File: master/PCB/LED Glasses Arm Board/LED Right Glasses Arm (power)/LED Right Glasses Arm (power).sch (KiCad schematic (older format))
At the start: 26 parts, among them J1 Conn_01x02_Male, J2 Conn_01x01_Male, J3 Conn_01x01_Male, Q1 TP0610T, SW1 SW_SPST, U1 TPS63061DSCT

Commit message: Changes
Test points, routing, need to get the ground plane on the back copper
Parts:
- TP_gnd1, TP_input_voltage1, TP_output_voltage1: footprint Connector_PinHeader_1.00mm:PinHeader_1x01_P1.00mm_Vertical_SMD_CUSTOM -> TestPoint:TestPoint_Pad_D1.5mm
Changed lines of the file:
@@
 F 0 "TP_output_voltage1" H 10058 4170 50  0000 L CNN
 F 1 "TestPoint" H 10058 4079 50  0000 L CNN
-F 2 "Connector_PinHeader_1.00mm:PinHeader_1x01_P1.00mm_Vertical_SMD_CUSTOM" H 10200 4050 50  0001 C CNN
+F 2 "TestPoint:TestPoint_Pad_D1.5mm" H 10200 4050 50  0001 C CNN
 F 3 "~" H 10200 4050 50  0001 C CNN
 	1    10000 4050
@@
 F 0 "TP_input_voltage1" H 2408 4120 50  0000 L CNN
 F 1 "TestPoint" H 2408 4029 50  0000 L CNN
-F 2 "Connector_PinHeader_1.00mm:PinHeader_1x01_P1.00mm_Vertical_SMD_CUSTOM" H 2550 4000 50  0001 C CNN
+F 2 "TestPoint:TestPoint_Pad_D1.5mm" H 2550 4000 50  0001 C CNN
 F 3 "~" H 2550 4000 50  0001 C CNN
 	1    2350 4000
@@
 F 0 "TP_gnd1" H 5108 5470 50  0000 L CNN
 F 1 "TestPoint" H 5108 5379 50  0000 L CNN
-F 2 "Connector_PinHeader_1.00mm:PinHeader_1x01_P1.00mm_Vertical_SMD_CUSTOM" H 5250 5350 50  0001 C CNN
+F 2 "TestPoint:TestPoint_Pad_D1.5mm" H 5250 5350 50  0001 C CNN
 F 3 "~" H 5250 5350 50  0001 C CNN
 	1    5050 5350

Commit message: Made a few small cosmetic changes to labels and values (i.e. R_small_US1 to R1).
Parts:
- C1, C4, C7, C8: value 220uF -> 220u; Digikey Link (none) -> https://www.digikey.com.au/product-detail/en/samsung-electr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; Link https://www.digikey.com.au/product-detail/en/samsung-electr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 -> (none)
- C2: Digikey Link (none) -> https://www.digikey.com.au/product-detail/en/samsung-electr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; Link https://www.digikey.com.au/product-detail/en/samsung-electr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 -> (none)
- C3: value 10pF -> 10p; Digikey Link (none) -> https://www.digikey.com.au/product-detail/en/avx-corporatio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; Link https://www.digikey.com.au/product-detail/en/avx-corporatio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 -> (none)
- C5: value 22uF -> 22u; Digikey Link (none) -> https://www.digikey.com.au/product-detail/en/kemet/C0805C22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; Link https://www.digikey.com.au/product-detail/en/kemet/C0805C22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 -> (none)
- C6: value 68uF -> 68u; Digikey Link (none) -> https://www.digikey.com.au/product-detail/en/tdk-corporatio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; Link https://www.digikey.com.au/product-detail/en/tdk-corporatio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 -> (none)
- D1: renamed from D_Zener_Small1; Digikey Link (none) -> https://www.digikey.com.au/product-detail/en/vishay-general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; Digikey link https://www.digikey.com.au/product-detail/en/vishay-general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 -> (none)
- D2: value LED Red -> P_IN
- D3: value LED Green -> P_OUT
- J1: value Conn_01x02_Male -> PWR IN
- J2: value Conn_01x01_Male -> PWR OUT +
- J3: value Conn_01x01_Male -> PWR OUT -
- L1: value 1uF -> 1u; Digikey https://www.digikey.com/en/products/detail/bourns-inc/SRN40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 -> (none); Digikey Link (none) -> https://www.digikey.com/en/products/detail/bourns-inc/SRN40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
- R1: renamed from R_Small_US1; symbol Device:R_Small_US -> LED-Right-Glasses-Arm-(power)-rescue:R_Small_US-Device
- R2, R3, R4, R6: symbol Device:R_Small_US -> LED-Right-Glasses-Arm-(power)-rescue:R_Small_US-Device
- SW1: value SW_SPST -> EN
- TP1: renamed from TP_input_voltage1; value TestPoint -> VIN
- TP2: renamed from TP_gnd1; value TestPoint -> GND
- TP3: renamed from TP_output_voltage1; value TestPoint -> VOUT

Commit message: All changes apply to schematic only and not to the layout. Removed external feedback loop, replaced bulk output capacitance with 3x22uF caps for cost savings and removed led indicator on input power.
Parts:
- removed C1, C4, C7, C8: 220u, Capacitor_SMD:C_1210_3225Metric, symbol Device:C_Small
- removed C3: 10p, Capacitor_SMD:C_0603_1608Metric, symbol Device:C_Small
- removed D2: P_IN, LED_SMD:LED_0603_1608Metric, symbol Device:LED
- removed R2: 2k2, Resistor_SMD:R_0603_1608Metric, symbol LED-Right-Glasses-Arm-(power)-rescue:R_Small_US-Device
- removed R3: 1M, Resistor_SMD:R_0603_1608Metric, symbol LED-Right-Glasses-Arm-(power)-rescue:R_Small_US-Device
- removed R4: 111k, Resistor_SMD:R_0805_2012Metric, symbol LED-Right-Glasses-Arm-(power)-rescue:R_Small_US-Device
- added C? (x2): 22u, Capacitor_SMD:C_1206_3216Metric, symbol Device:C_Small
- added R2: 100k, Resistor_SMD:R_0603_1608Metric, symbol Device:R_Small
- C5: Digikey Link https://www.digikey.com.au/product-detail/en/kemet/C0805C22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 -> https://www.digikey.com.au/product-detail/en/samsung-electr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
- C6: value 68u -> 22u; Digikey Link https://www.digikey.com.au/product-detail/en/tdk-corporatio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 -> https://www.digikey.com.au/product-detail/en/samsung-electr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
- L1: Digikey Link https://www.digikey.com/en/products/detail/bourns-inc/SRN40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 -> https://www.digikey.com.au/product-detail/en/taiyo-yuden/NR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; Old product XFL4020-102MEC -> (none)
- R1: value 100k1 -> 100k; symbol LED-Right-Glasses-Arm-(power)-rescue:R_Small_US-Device -> Device:R_Small
- R6: symbol LED-Right-Glasses-Arm-(power)-rescue:R_Small_US-Device -> Device:R_Small
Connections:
- net labels added: 5V0
- net labels removed: VOUT_5V
- wire segments 64 -> 42
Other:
- moved on the sheet: C2, C5, C6, D3, J2, J3, SW1, TP2, TP3

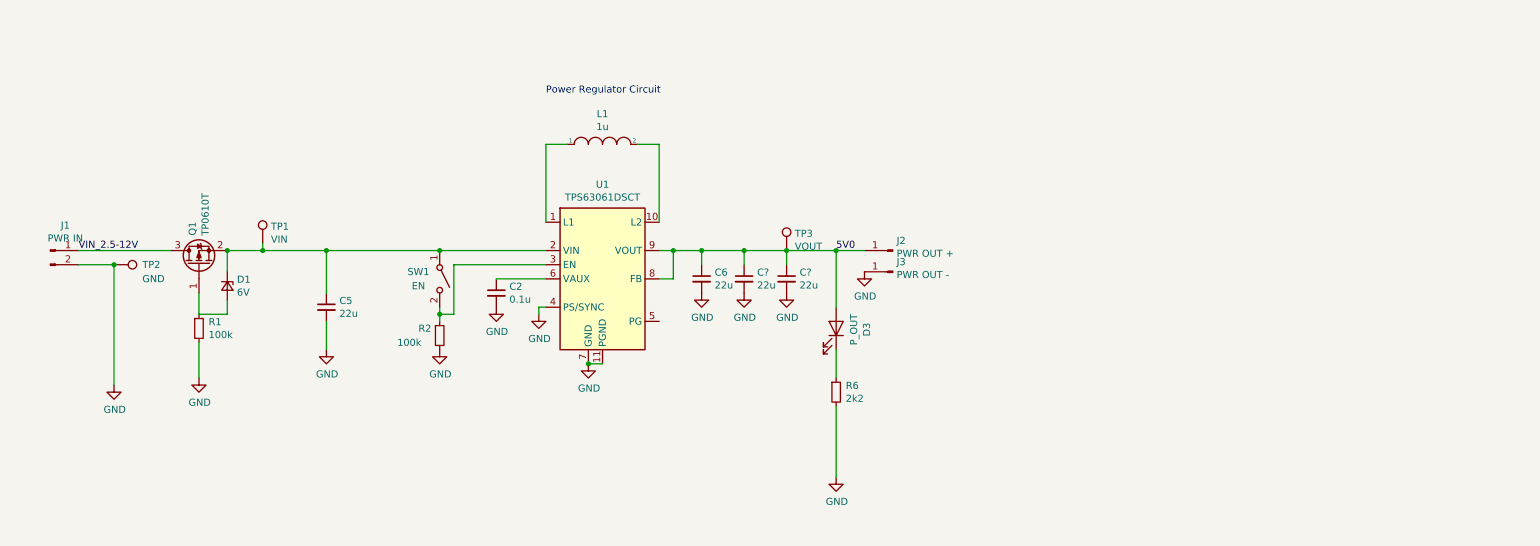
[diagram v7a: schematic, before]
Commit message: Changed LED indicator from 5V out to PG from power reg IC, moved annotation from 0-x to 100-1xx to keep it consistent with mcu arm design, adjusted layout to accomodate schematic changes from this commit and the previous and added silkscreen labels to input and output.
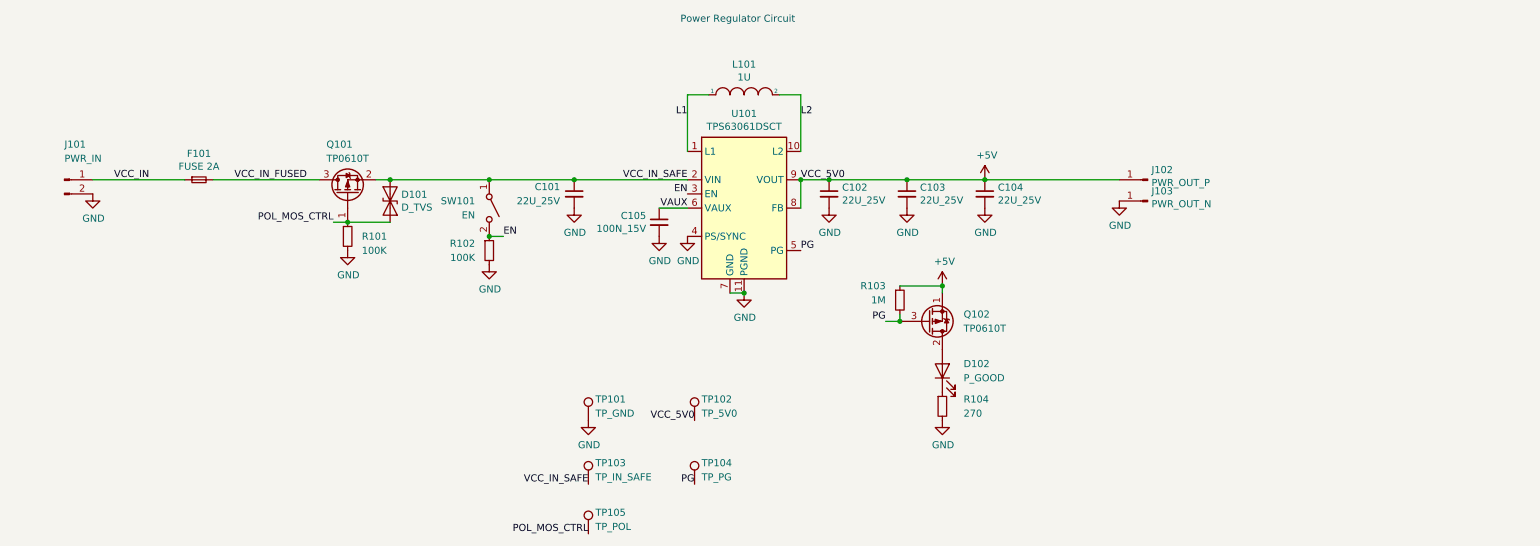
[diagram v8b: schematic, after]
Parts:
- removed D1: 6V, Diode_SMD:D_SOD-123, symbol Device:D_Zener_Small
- removed TP1: VIN, TestPoint:TestPoint_Pad_D1.5mm, symbol Connector:TestPoint
- removed TP2: GND, TestPoint:TestPoint_Pad_D1.5mm, symbol Connector:TestPoint
- removed TP3: VOUT, TestPoint:TestPoint_Pad_D1.5mm, symbol Connector:TestPoint
- added D101: D_TVS, Diode_SMD:D_SOD-323, symbol Device:D_TVS
- added F101: FUSE 2A, Resistor_SMD:R_1206_3216Metric, symbol Device:Fuse_Small
- added Q102: TP0610T, Package_TO_SOT_SMD:SOT-23, symbol Device:Q_PMOS_SDG
- added R103: 1M, Resistor_SMD:R_0805_2012Metric, symbol Device:R_Small
- added TP101: TP_GND, TestPoint:TestPoint_Pad_D1.0mm, symbol Connector:TestPoint
- added TP102: TP_5V0, TestPoint:TestPoint_Pad_D1.0mm, symbol Connector:TestPoint
- added TP103: TP_IN_SAFE, TestPoint:TestPoint_Pad_D1.0mm, symbol Connector:TestPoint
- added TP104: TP_PG, TestPoint:TestPoint_Pad_D1.0mm, symbol Connector:TestPoint
- added TP105: TP_POL, TestPoint:TestPoint_Pad_D1.0mm, symbol Connector:TestPoint
- C101: renamed from C5; value 22u -> 22U_25V; Description (none) -> 22UF ±20% 25V X5R 0805 (2012 Metric); Digi-Key Part Number (none) -> 1276-CL21A226MAYNNNECT-ND
- C102: renamed from C6; value 22u -> 22U_25V; footprint Capacitor_SMD:C_1206_3216Metric -> Capacitor_SMD:C_0805_2012Metric; Description (none) -> 22UF ±20% 25V X5R 0805 (2012 Metric); Digi-Key Part Number (none) -> 1276-CL21A226MAYNNNECT-ND
- C103, C104: renamed from C?; value 22u -> 22U_25V; footprint Capacitor_SMD:C_1206_3216Metric -> Capacitor_SMD:C_0805_2012Metric; Description (none) -> 22UF ±20% 25V X5R 0805 (2012 Metric); Digi-Key Part Number (none) -> 1276-CL21A226MAYNNNECT-ND
- C105: renamed from C2; value 0.1u -> 100N_15V; footprint Capacitor_SMD:C_0402_1005Metric -> Capacitor_SMD:C_0805_2012Metric; Description (none) -> 0.1µF ±20% 25V X7R 0805 (2012 Metric); Digi-Key Part Number (none) -> 399-8000-1-ND; Digikey Link https://www.digikey.com.au/product-detail/en/samsung-electr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 -> https://www.digikey.com.au/product-detail/en/kemet/C0805C10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
- D102: renamed from D3; value P_OUT -> P_GOOD; footprint LED_SMD:LED_0603_1608Metric -> LED_SMD:LED_0805_2012Metric; Description (none) -> LED GREEN CLEAR 0805 SMD; Digi-Key Part Number (none) -> 732-4986-1-ND; Digikey Link https://www.digikey.com.au/product-detail/en/lite-on-inc/LT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 -> https://www.digikey.com.au/product-detail/en/w%C3%BCrth-ele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
- J101: renamed from J1; value PWR IN -> PWR_IN; Digikey Link https://www.digikey.com.au/product-detail/en/jst-sales-amer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 -> https://au.element14.com/jst-japan-solderless-terminals/s2b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; Link https://au.element14.com/jst-japan-solderless-terminals/s2b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 -> (none)
- J102: renamed from J2; value PWR OUT + -> PWR_OUT_P
- J103: renamed from J3; value PWR OUT - -> PWR_OUT_N
- L101: renamed from L1; value 1u -> 1U; footprint sft:SRN4018TA -> Inductor_SMD:L_Taiyo-Yuden_NR-50xx_HandSoldering; Description (none) -> FIXED IND 1UH 3.6A 25.2 MOHM SMD; Digi-Key Part Number (none) -> 587-2403-1-ND
- Q101: renamed from Q1; Description (none) -> MOSFET P-CH 12V 3A SOT23-3; Digi-Key Part Number (none) -> SI2315BDS-T1-GE3CT-ND
- R101: renamed from R1; value 100k -> 100K; footprint Resistor_SMD:R_0603_1608Metric -> Resistor_SMD:R_0805_2012Metric; Description (none) -> RES SMD 100K OHM 0.5% 1/10W 0805; Digi-Key Part Number (none) -> RR12P100KDCT-ND; Digikey Link https://www.digikey.com.au/product-detail/en/susumu/RR0816P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 -> https://www.digikey.com.au/product-detail/en/susumu/RR1220P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
- R102: renamed from R2; value 100k -> 100K; footprint Resistor_SMD:R_0603_1608Metric -> Resistor_SMD:R_0805_2012Metric; Description (none) -> RES SMD 100K OHM 0.5% 1/10W 0805; Digi-Key Part Number (none) -> RR12P100KDCT-ND; Digikey Link https://www.digikey.com.au/product-detail/en/susumu/RR0816P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 -> https://www.digikey.com.au/product-detail/en/susumu/RR1220P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
- R104: renamed from R6; value 2k2 -> 270; footprint Resistor_SMD:R_0603_1608Metric -> Resistor_SMD:R_0805_2012Metric; Description (none) -> RES SMD 270 OHM 0.5% 1/10W 0805; Digi-Key Part Number (none) -> RR12P270DCT-ND; Digikey Link https://www.digikey.com.au/product-detail/en/te-connectivit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 -> https://www.digikey.com.au/product-detail/en/susumu/RR1220P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
- SW101: renamed from SW1; Description (none) -> SWITCH SLIDE DPDT 300MA 6V; Digi-Key Part Number (none) -> 401-2002-1-ND
- U101: renamed from U1; Description (none) -> IC REG BCK BST 5V 2A 10WSON; Digi-Key Part Number (none) -> 296-30179-1-ND
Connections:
- net GND: now also TP101.1
- net L1: now reaches L101.1, U101.1 (L1)
- net L2: now reaches L101.2, U101.10 (L2)
- net VCC_IN_SAFE: now reaches C101.1, Q101.2 (S), SW101.1 (A), U101.2 (VIN)
- net VCC_IN_SAFE: now also D101.1 (A1), TP103.1
- net EN: now reaches R102.1, SW101.2 (B), U101.3 (EN)
- net PG: now reaches U101.5 (PG)
- net PG: now also Q102.3 (G), R103.2, TP104.1
- net VAUX: now reaches C105.1, U101.6 (VAUX)
- net POL_MOS_CTRL: now reaches Q101.1 (G), R101.1
- net POL_MOS_CTRL: now also D101.2 (A2), TP105.1
- net 5V0 renamed +5V
- net +5V: now also Q102.1 (S), R103.1, TP102.1; no longer D102.2 (A)
- net VIN_2.5-12V renamed VCC_IN
- net VCC_IN: now also F101.1; no longer Q101.3 (D)
- new net: D102.2 (A), Q102.2 (D)
- new net VCC_IN_FUSED: F101.2, Q101.3 (D)
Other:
- moved on the sheet: C101, C102, C103, C104, C105, D102, J101, J102, J103, L101, Q101, R101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
